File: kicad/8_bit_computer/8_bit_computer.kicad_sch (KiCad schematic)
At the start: 0 parts

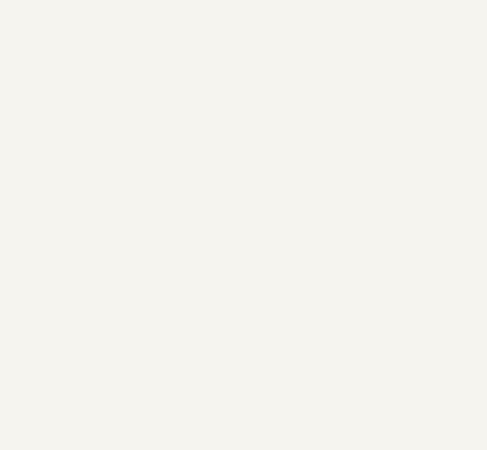
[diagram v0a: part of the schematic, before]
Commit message: Astable clock
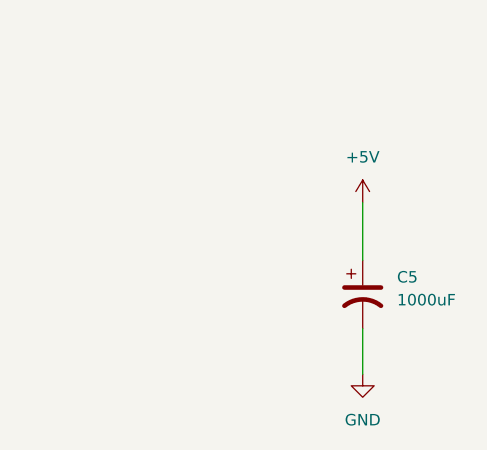
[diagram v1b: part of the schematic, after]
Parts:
- added C5: 1000uF, Capacitor_THT:CP_Radial_D12.5mm_P5.00mm, symbol Device:C_Polarized_US
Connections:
- new net +5V: C5.1
- new net GND: C5.2

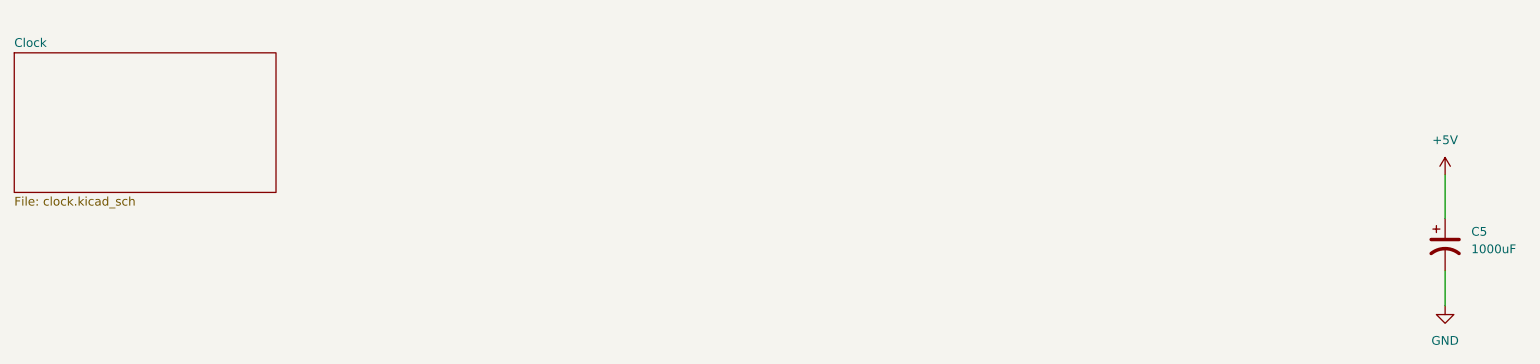
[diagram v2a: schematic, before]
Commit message: Mostly implemented register, still ERC errors
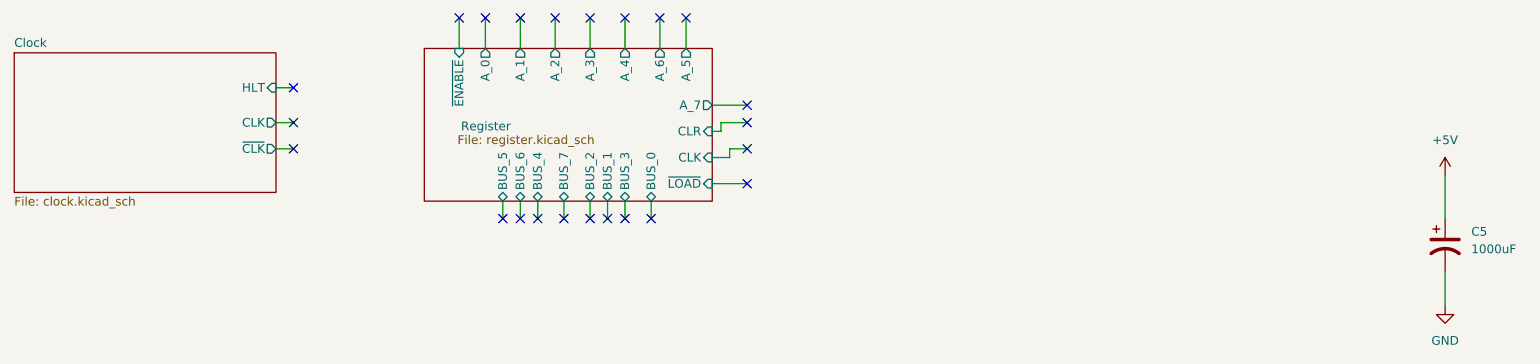
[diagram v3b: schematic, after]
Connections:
- no-connect marks 0 -> 23
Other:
- added sheet Register (register.kicad_sch)
- sheet Clock ports: added CLK, HLT, ~{CLK}; removed none
